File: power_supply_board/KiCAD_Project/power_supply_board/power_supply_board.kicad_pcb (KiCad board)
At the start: 2 copper layers, 50.8 x 33 mm, 7 parts, among them J1 To Digitiziers, J2 Power Input, U1 TDN 5-2411WI

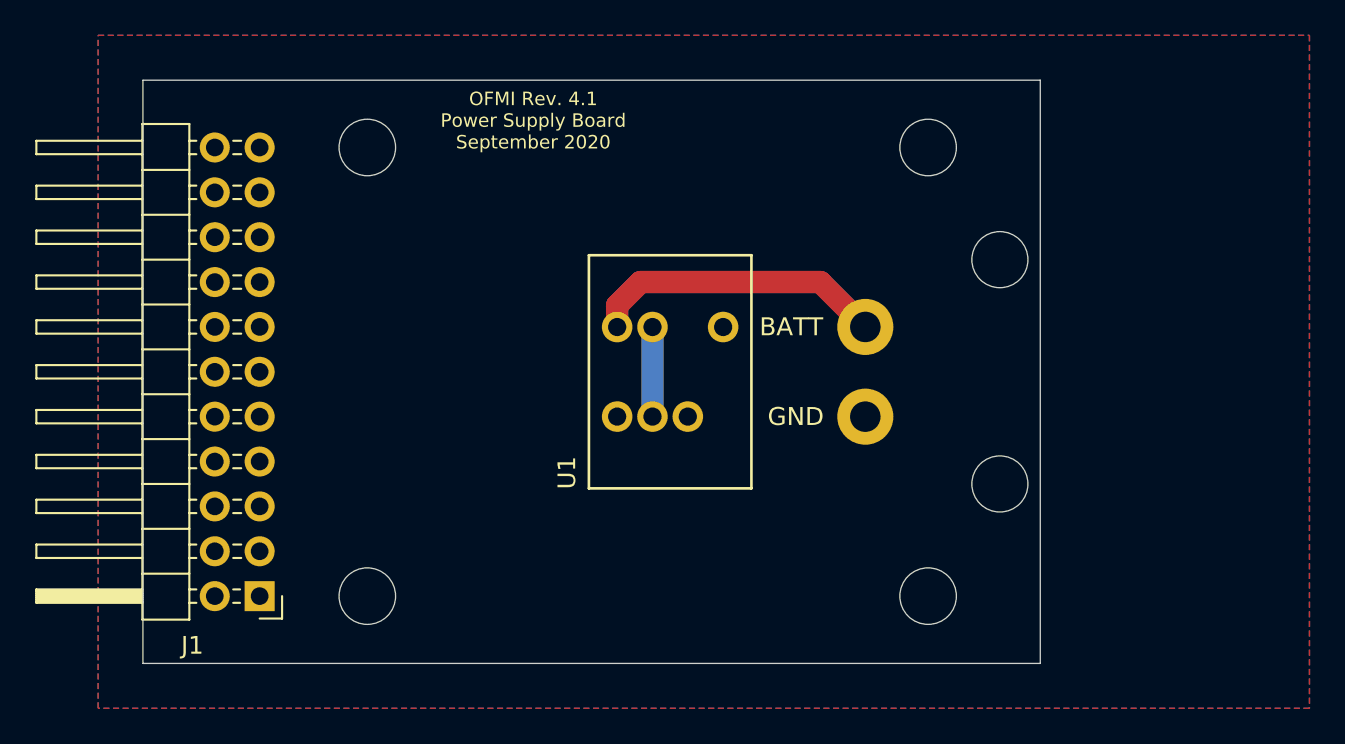
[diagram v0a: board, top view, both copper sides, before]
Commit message: Update power supply board to Rev 4.2. Closes #32.
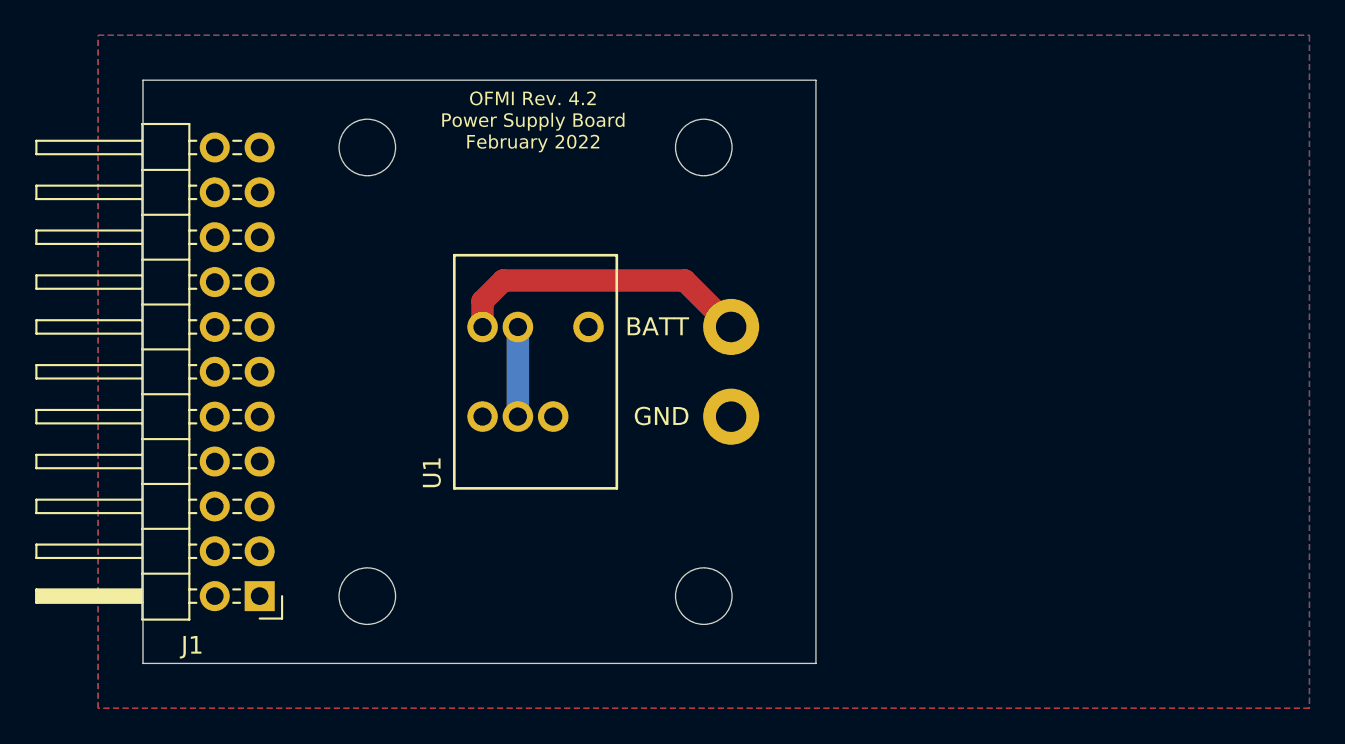
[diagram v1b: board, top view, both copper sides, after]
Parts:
- added PCB1: barepcb, misc:barepcb, F.Cu at (159.1, 134.7)
- moved H2 12.7 mm to (156.2, 102.9)
- moved H3 12.7 mm to (156.2, 128.3)
- moved U1 7.62 mm to (146.7, 115.6)
- moved J2 7.59 mm to (157.8, 115.6)
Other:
- board size 50.8 x 33 mm -> 38.1 x 33 mm
- rule pad_to_mask_clearance: 0.0508 -> 0
- board text added: "3-0000124"
- board text added: "OFMI Rev. 4.2 Power Supply Board February 2022"
- board text removed: "+5"
- board text removed: "CS"
- board text removed: "LG 3-0000044"
- board text removed: "MISO1"
- board text removed: "MISO2"
- board text removed: "MISO3"
- board text removed: "MISO4"
- board text removed: "MISO5"
- board text removed: "MISO6"
- board text removed: "MISO7"
- board text removed: "MISO8"
- board text removed: "MISO9"
- board text removed: "MOSI"
- board text removed: "NC"
- board text removed: "OFMI Rev. 4.1 Power Supply Board September 2020"
- board text removed: "SCLK"

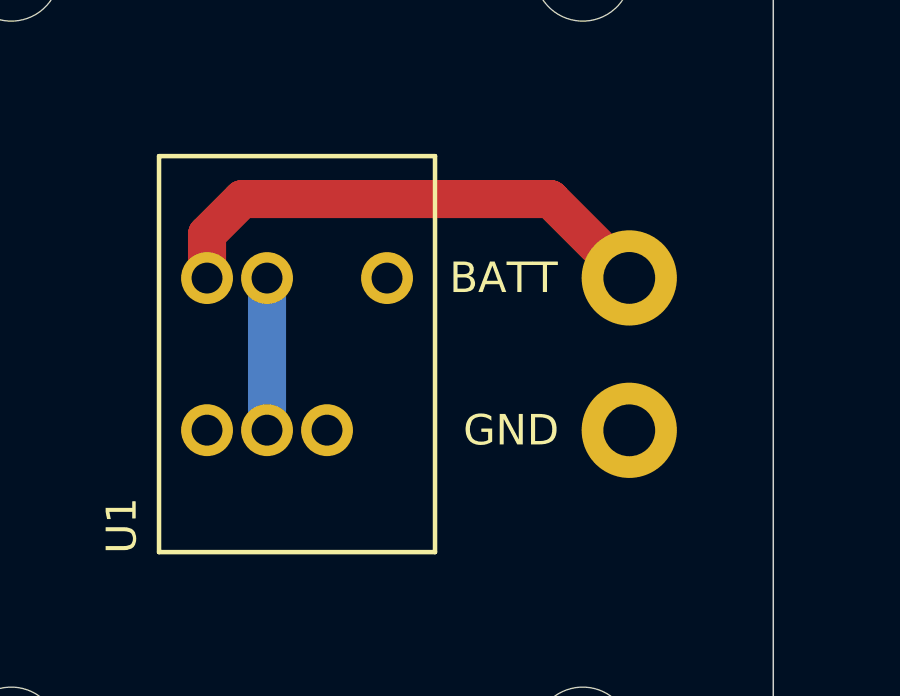
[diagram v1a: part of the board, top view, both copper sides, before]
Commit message: Move pads apart for wire entry on power supply board
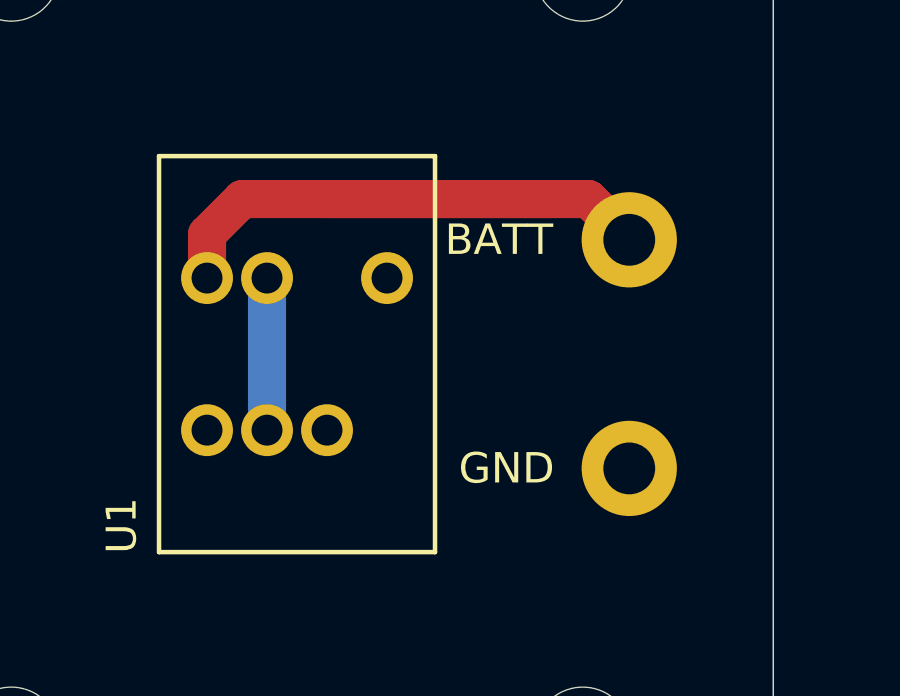
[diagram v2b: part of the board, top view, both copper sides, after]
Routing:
- net +BATT: track 17.1 -> 24.1 mm
